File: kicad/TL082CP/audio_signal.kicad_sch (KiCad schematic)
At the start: 7 parts, among them U2 TL082

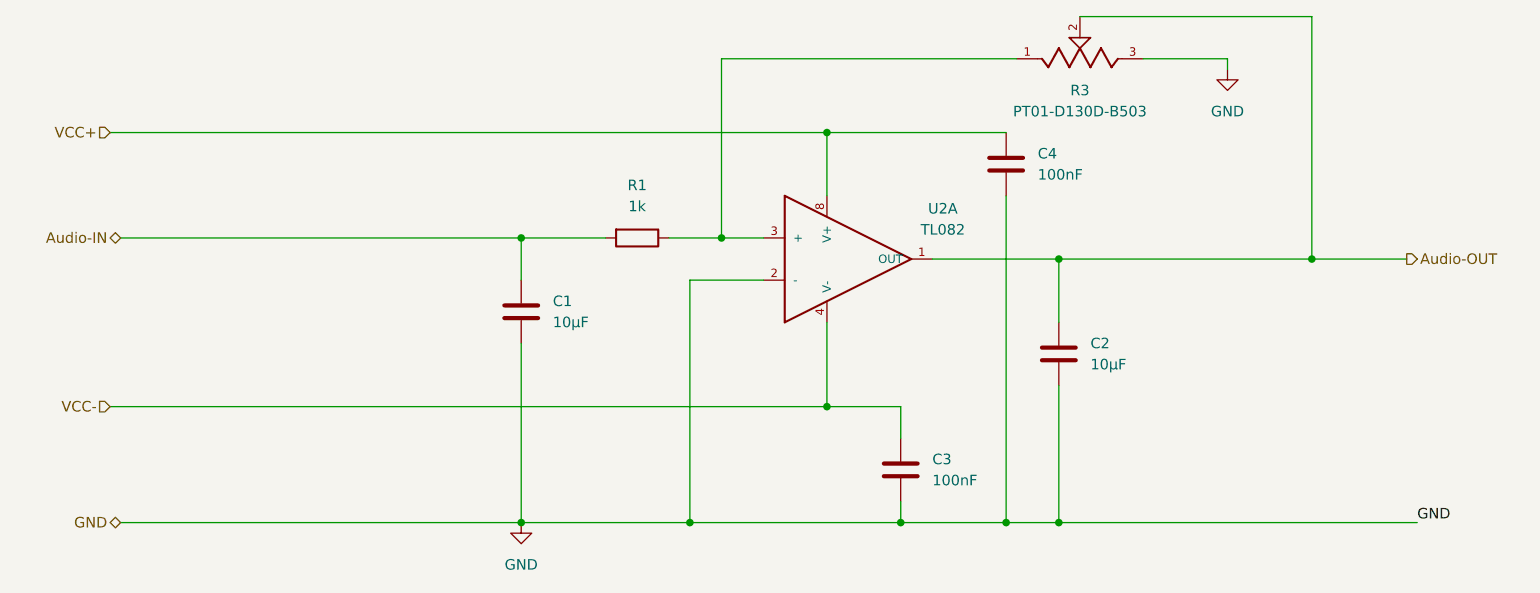
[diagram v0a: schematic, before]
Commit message: fix: schematic capacitors, resistors, symbols updated
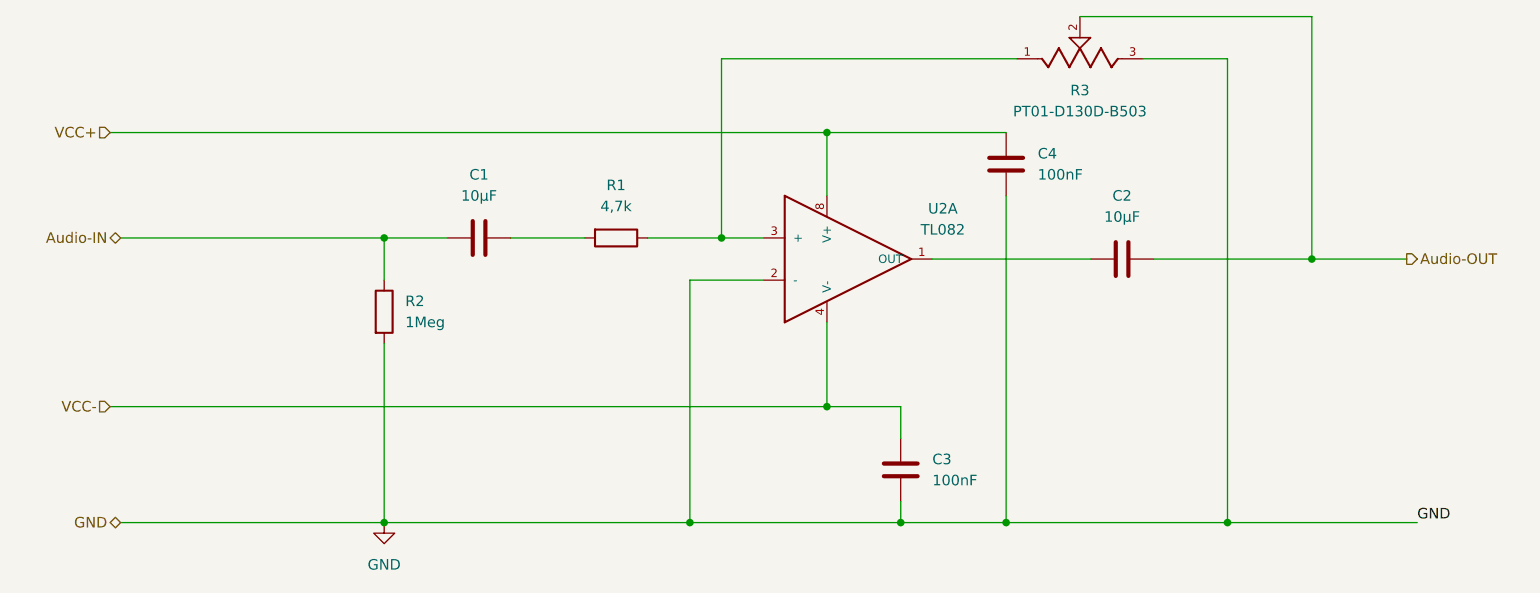
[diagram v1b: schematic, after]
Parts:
- added R2: 1Meg, Resistor_THT:R_Axial_DIN0207_L6.3mm_D2.5mm_P7.62mm_Horizontal, symbol Device:R
- R1: value 1k -> 4,7k
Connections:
- net Audio-IN: now also R2.1; no longer R1.2
- net Audio-OUT: now also C2.2; no longer C2.1, U2.1 (OUT)
- net GND: now also R2.2; no longer C1.2, C2.2
- new net: C1.2, R1.2
- new net: C2.1, U2.1 (OUT)
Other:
- moved on the sheet: C1, C2, R1
